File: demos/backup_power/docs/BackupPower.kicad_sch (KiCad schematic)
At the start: 21 parts, among them U2 LM5002

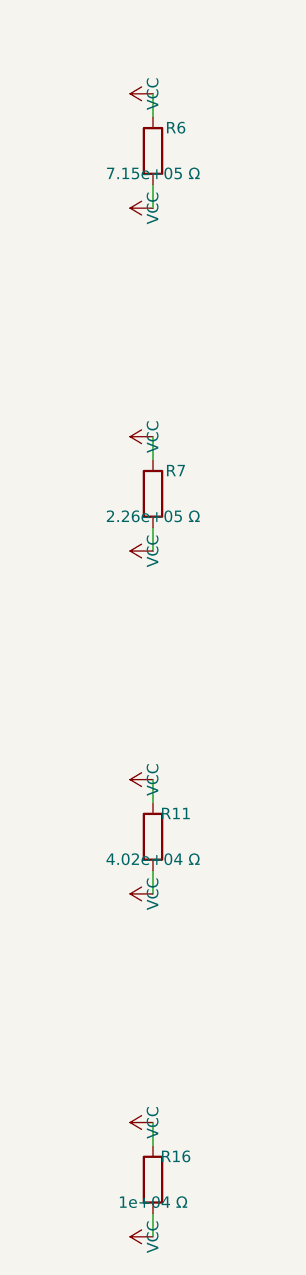
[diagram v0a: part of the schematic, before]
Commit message: units: Ohms.__str__ uses engineering notation (kΩ, MΩ, GΩ)
The previous `Ohms.__str__` formatted with bare `:.3g`, producing
unreadable scientific output for clean kilo / mega multiples:

  str(Ohms(10_000))     == "1e+04 Ω"      → now "10 kΩ"
  str(Ohms(100_000))    == "1e+05 Ω"      → now "100 kΩ"
  str(Ohms(1_000_000))  == "1e+06 Ω"      → now "1 MΩ"

The breadboard SVG visualiser surfaced the problem: a resistor body
labelled "100000Ω" makes a reader count zeros, while a label of
"100 kΩ" reads at a glance — exactly the convention every schematic
and parts catalogue uses. Centralising the engineering notation in
`Ohms.__str__` means every downstream consumer (assembly guide,
breadboard SVG, kicad netlist, BOM, reports) inherits the readable
form without each format adapter rolling its own formatter.

  - `Ohms.__str__` returns "47 Ω", "4.7 kΩ", "10 kΩ", "100 kΩ",
    "1 MΩ", "10 MΩ", "1 GΩ" per the kilo / mega / giga thresholds.
  - `Resistor.__str__` delegates to `str(self._ohms)` so it
    inherits the new notation (was producing the noisy "47.0 Ω"
    via raw float).
  - The breadboard visualiser's resistor body label uses
    `str(part.ohms)` directly (previously had a private
    `_format_ohms_compact` helper; removed).
  - `tests/components/test_resistor.py::test_str` updated for
    "47 Ω" (was "47.0 Ω"); new `test_str_renders_in_engineering_notation`
    pins kΩ / MΩ output across the kilo and mega thresholds.
  - All demo docs / goldens refreshed where the Ohms.__str__
    change affected the rendered output (breadboard SVGs, kicad
    sch value fields, BOM rows).
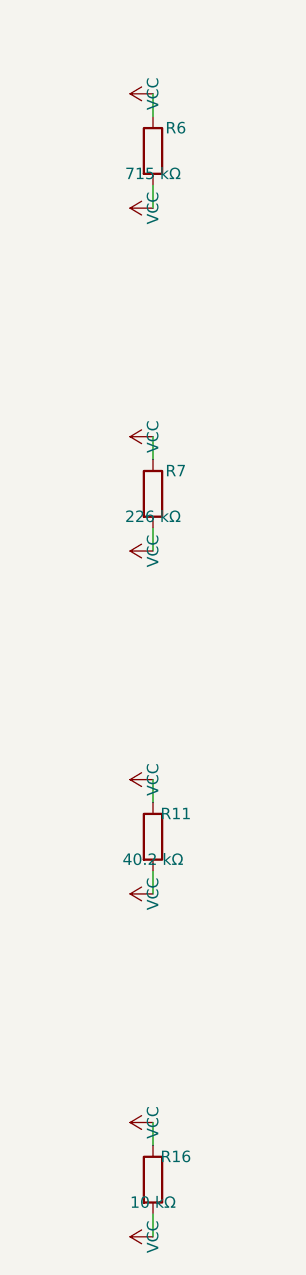
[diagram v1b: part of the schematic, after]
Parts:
- R11: value 4.02e+04 Ω -> 40.2 kΩ
- R16: value 1e+04 Ω -> 10 kΩ
- R6: value 7.15e+05 Ω -> 715 kΩ
- R7: value 2.26e+05 Ω -> 226 kΩ
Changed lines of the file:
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@@
       (effects (font (size 1.27 1.27)))
     )
-    (property "Value" "7.15e+05 Ω"
+    (property "Value" "715 kΩ"
       (at 63.5 967.74 0)
       (effects (font (size 1.27 1.27)))
@@
       (effects (font (size 1.27 1.27)))
     )
-    (property "Value" "2.26e+05 Ω"
+    (property "Value" "226 kΩ"
       (at 63.5 1005.84 0)
       (effects (font (size 1.27 1.27)))
@@
       (effects (font (size 1.27 1.27)))
     )
-    (property "Value" "4.02e+04 Ω"
+    (property "Value" "40.2 kΩ"
       (at 63.5 1043.94 0)
       (effects (font (size 1.27 1.27)))
@@
       (effects (font (size 1.27 1.27)))
     )
-    (property "Value" "1e+04 Ω"
+    (property "Value" "10 kΩ"
       (at 63.5 1082.04 0)
       (effects (font (size 1.27 1.27)))

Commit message: units: Farads + Henries __str__ also use engineering notation
Same treatment as `Ohms.__str__` (previous commit) for the other two
passive engineering quantities. Demos contain caps and inductors
with values that the bare `:.3g` formatter would emit in scientific
form (`1e-07 F` for a 100 nF decoupling cap); centralising the
engineering notation on the unit class means every consumer
(reports, BOM, breadboard SVG, etc.) inherits the readable form.

  - `Farads.__str__` returns `100 pF`, `22 nF`, `100 nF`, `1 µF`,
    `4.7 µF`, `470 µF`, `1 mF`, `1 F` across the standard
    capacitance bands.
  - `Henries.__str__` returns `100 nH`, `10 µH`, `22 mH`, `1 H`
    across the standard inductance bands.
  - `Capacitor.__str__` and `Inductor.__str__` delegate to the
    unit class's str (were rolling raw-float formatters).
  - `framework.export.reports_common.part_description` now uses
    `str(part.ohms / farads / henries)` directly instead of the
    parallel `_format_ohms` / `_format_farads` / `_format_henries`
    helpers (removed — they duplicated the new logic on raw
    floats).
  - Breadboard SVG renderer now also labels capacitor and inductor
    bodies with their engineering-notation value (was only
    resistors).
  - `tests/framework/test_units.py`: parametrised regression tests
    for both unit classes across every band.
  - All affected demo docs / goldens refreshed.
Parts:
- C1: value 1e-08 F -> 10 nF
- C10: value 0.0012 F -> 1.2 mF
- C12, C14, C2, C3, C6, C8: value 1e-06 F -> 1 µF
- C13: value 0.00022 F -> 220 µF
- C15: value 2.2e-06 F -> 2.2 µF
- C4: value 3.3e-09 F -> 3.3 nF
- C5: value 2.2e-08 F -> 22 nF
- C7, C9: value 1e-07 F -> 100 nF
- L1: value 3.3e-05 H -> 33 µH
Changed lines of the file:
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@@
       (effects (font (size 1.27 1.27)))
     )
-    (property "Value" "3.3e-05 H"
+    (property "Value" "33 µH"
       (at 63.5 929.64 0)
       (effects (font (size 1.27 1.27)))
@@
       (effects (font (size 1.27 1.27)))
     )
-    (property "Value" "0.0012 F"
+    (property "Value" "1.2 mF"
       (at 63.5 472.44 0)
       (effects (font (size 1.27 1.27)))
@@
       (effects (font (size 1.27 1.27)))
     )
-    (property "Value" "1e-08 F"
+    (property "Value" "10 nF"
       (at 63.5 129.54 0)
       (effects (font (size 1.27 1.27)))
@@
       (effects (font (size 1.27 1.27)))
     )
-    (property "Value" "1e-06 F"
+    (property "Value" "1 µF"
       (at 63.5 167.64 0)
       (effects (font (size 1.27 1.27)))
@@
       (effects (font (size 1.27 1.27)))
     )
-    (property "Value" "1e-06 F"
+    (property "Value" "1 µF"
       (at 63.5 205.74 0)
       (effects (font (size 1.27 1.27)))
@@
       (effects (font (size 1.27 1.27)))
     )
-    (property "Value" "3.3e-09 F"
+    (property "Value" "3.3 nF"
       (at 63.5 243.84 0)
       (effects (font (size 1.27 1.27)))
@@
       (effects (font (size 1.27 1.27)))
     )
-    (property "Value" "2.2e-08 F"
+    (property "Value" "22 nF"
       (at 63.5 281.94 0)
       (effects (font (size 1.27 1.27)))
@@
       (effects (font (size 1.27 1.27)))
     )
-    (property "Value" "1e-06 F"
+    (property "Value" "1 µF"
       (at 63.5 320.04 0)
       (effects (font (size 1.27 1.27)))
@@
       (effects (font (size 1.27 1.27)))
     )
-    (property "Value" "1e-07 F"
+    (property "Value" "100 nF"
       (at 63.5 358.14 0)
       (effects (font (size 1.27 1.27)))
@@
       (effects (font (size 1.27 1.27)))
     )
-    (property "Value" "1e-06 F"
+    (property "Value" "1 µF"
       (at 63.5 396.24 0)
       (effects (font (size 1.27 1.27)))
@@
       (effects (font (size 1.27 1.27)))
     )
-    (property "Value" "1e-07 F"
+    (property "Value" "100 nF"
       (at 63.5 434.34 0)
       (effects (font (size 1.27 1.27)))
@@
       (effects (font (size 1.27 1.27)))
     )
-    (property "Value" "1e-06 F"
+    (property "Value" "1 µF"
       (at 63.5 510.54 0)
       (effects (font (size 1.27 1.27)))
@@
       (effects (font (size 1.27 1.27)))
     )
-    (property "Value" "0.00022 F"
+    (property "Value" "220 µF"
       (at 63.5 548.64 0)
       (effects (font (size 1.27 1.27)))
@@
       (effects (font (size 1.27 1.27)))
     )
-    (property "Value" "1e-06 F"
+    (property "Value" "1 µF"
       (at 63.5 586.74 0)
       (effects (font (size 1.27 1.27)))
@@
       (effects (font (size 1.27 1.27)))
     )
-    (property "Value" "2.2e-06 F"
+    (property "Value" "2.2 µF"
       (at 63.5 624.84 0)
       (effects (font (size 1.27 1.27)))
